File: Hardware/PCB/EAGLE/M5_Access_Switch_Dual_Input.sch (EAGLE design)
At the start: 13 parts

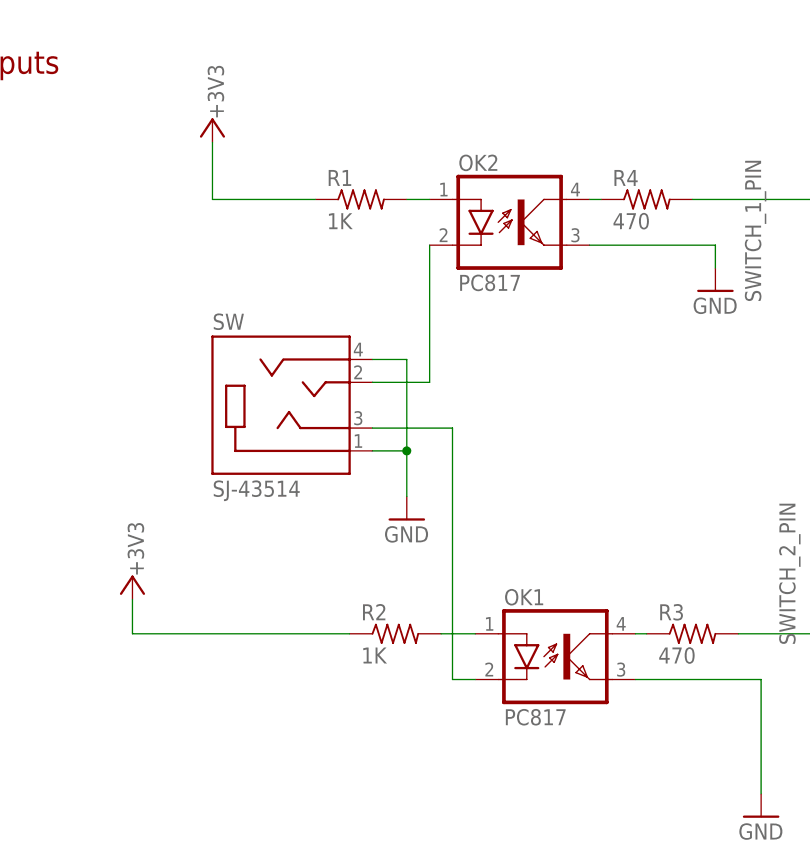
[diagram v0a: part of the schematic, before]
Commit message: Changed the design to dual mono jacks
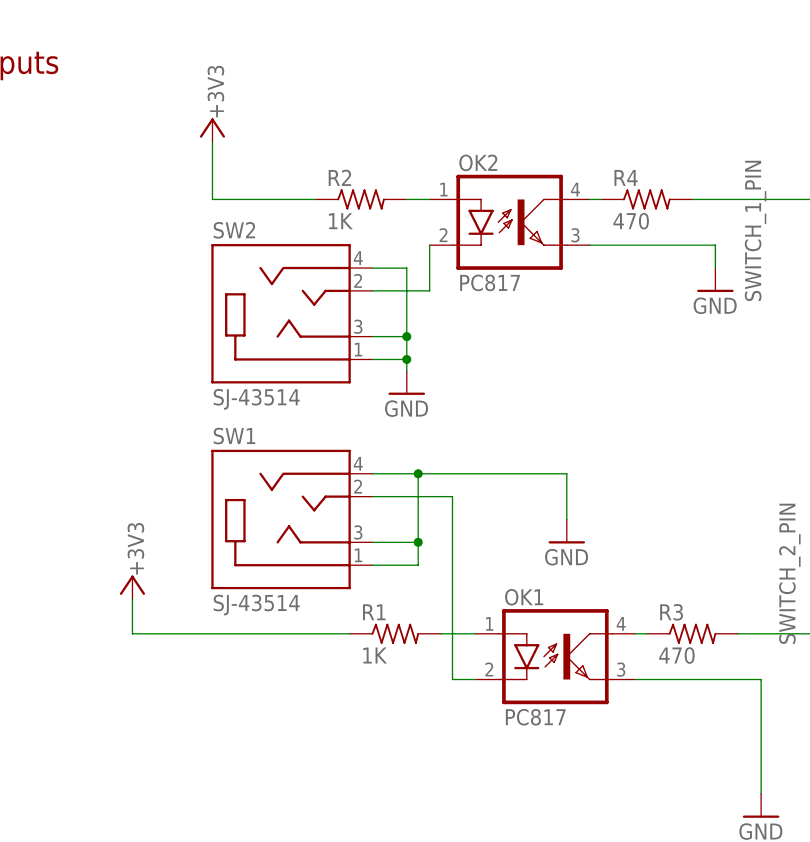
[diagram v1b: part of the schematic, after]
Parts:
- removed SW: SJ-43514, milador:SJ-43514
- added SW1, SW2: SJ-43514, milador:SJ-43514
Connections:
- net GND: now also SW1.RING1, SW1.RING2, SW1.SLEEVE, SW2.RING1, SW2.RING2, SW2.SLEEVE; no longer SW.RING2, SW.SLEEVE
- net N$1: now also R1.2; no longer R2.2
- net N$14: now also R2.2; no longer R1.2
- net N$23: now also SW2.TIP; no longer SW.TIP
- net N$3: now also SW1.TIP; no longer SW.RING1
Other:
- moved on the sheet: R1, R2
